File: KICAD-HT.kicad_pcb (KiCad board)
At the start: 2 copper layers, 85 x 70 mm, 124 parts, among them J1 HV80_IN, J2 NAPPE_FILAMENT_HT, Q1 IPD050N10N5, Q2 IPD050N10N5, Q3 BSS127I, Q4 MMBT2222, Q5 BSS127I, T1 MSD1514-103ME, U1 UCC27517, U10 ISO7710, U11 AMC0311R, U12 UCC24612, U13 SN74LVC1G08, U14 TSV791, U15 ATL431, U16 LMV7219, U17 SN74LVC1G132, U18 SN74LVC1G74, U19 ISO7710F, U3 ISO7710, U5 DPC817, U7 AMC0311R, U8 AMC0311R, U9 AMC0302R

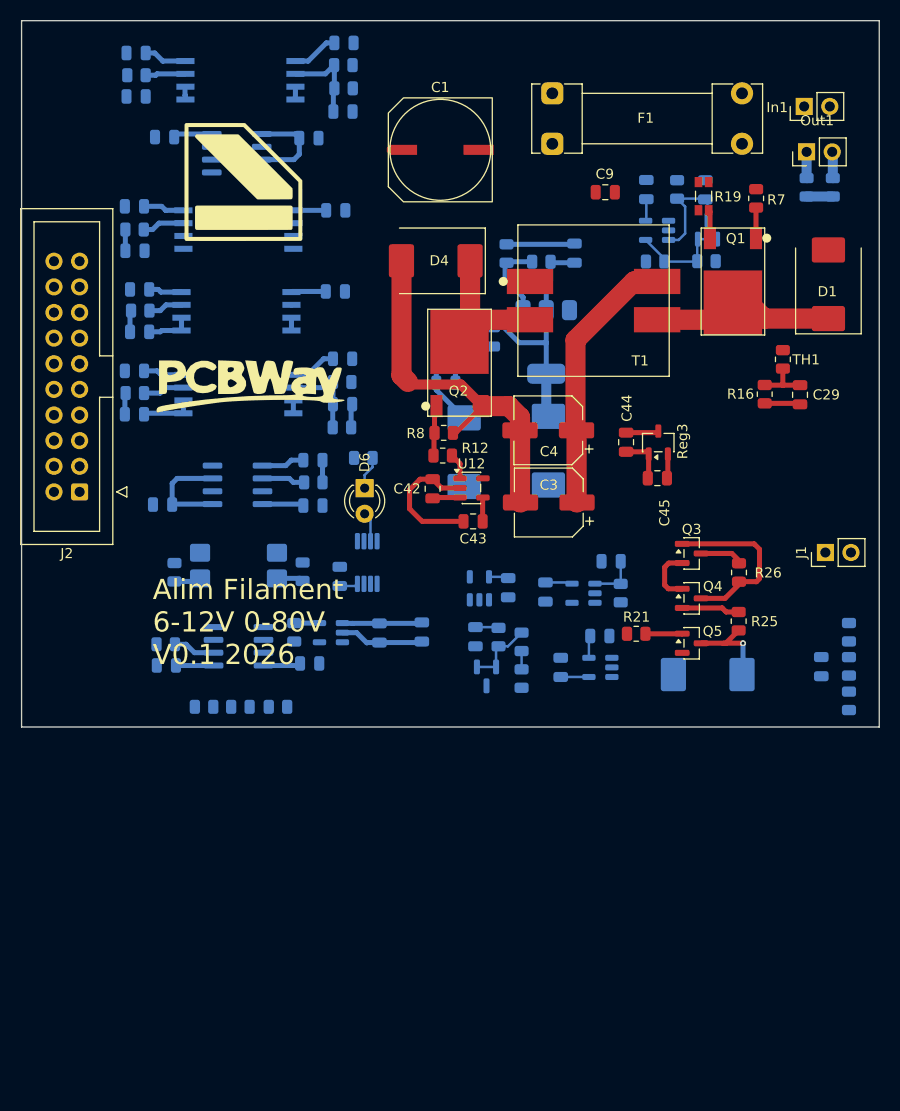
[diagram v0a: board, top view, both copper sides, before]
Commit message: Linearisation HV_BIAS : composants reels en simulation, correctif Rs+Cint
Rejoue la boucle de linearisation (MCP6001 + Q6/Q7) avec des modeles
reels (MMBF170, MCP6001 parametre depuis sa datasheet) plutot que des
modeles ideaux/generiques : revele une oscillation auto-entretenue
invisible sur le schema seul, confirmee independante du proxy MOSFET
et non liee a la bande passante de l'ampli-op (teste avec un TSV791
plus rapide, resultat pire).

Correctif valide en simulation avant report sur le schema : resistance
de degenerescence Rs=330 sur la source de Q6/Q7 (supprime l'oscillation
sans sacrifier l'acces a HV_BIAS=0V) + condensateur de compensation
Cint=1nF autour de l'ampli-op (supprime le depassement en echelon).
Report sur polarisation.kicad_sch et le PCB (R7).

Garde les scripts, modeles et courbes de l'investigation comme
historique de recherche (simulation/*.py, models/, plots/) ; les
sorties volumineuses regenerables (.raw/.csv dans results/) sont
exclues via .gitignore.

Co-Authored-By: Claude Sonnet 5 <noreply@anthropic.com>
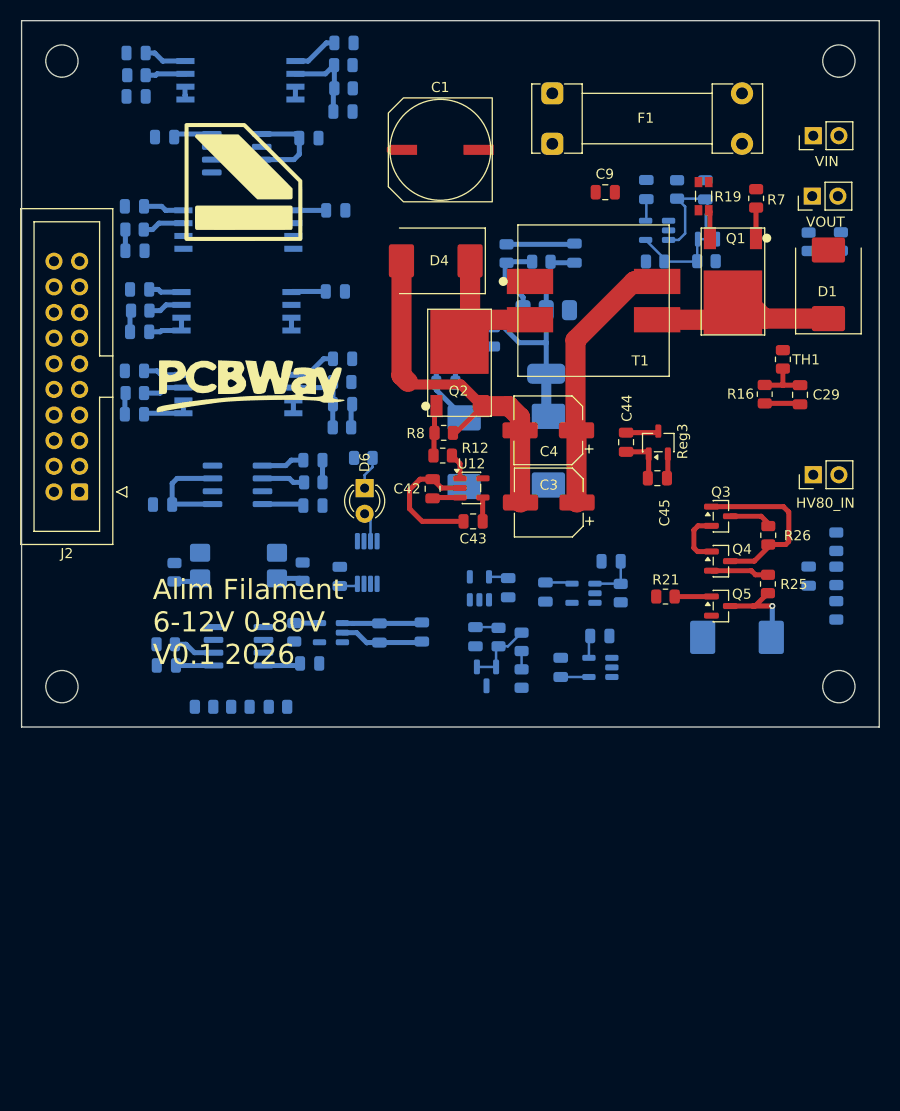
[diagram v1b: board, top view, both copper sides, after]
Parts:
- added ?: , , F.Cu at (176.0, 51.0)
- added ?: , , F.Cu at (176.0, 113.0)
- added REF**: MountingHole_3.2mm_M3, MountingHole:MountingHole_3.2mm_M3, F.Cu at (99.0, 113.0)
- added REF**: MountingHole_3.2mm_M3, MountingHole:MountingHole_3.2mm_M3, F.Cu at (99.0, 51.0)
- moved C27 9.05 mm to (173.0, 102.0)
- moved R40 9.05 mm to (175.7, 98.6)
- moved R41 9.05 mm to (175.7, 102.0)
- moved R42 9.05 mm to (175.7, 105.4)
- moved J1 7.80 mm to (173.5, 92.0)
- moved R10 5.43 mm to (176.2, 68.9)
- moved R9 5.40 mm to (173.0, 68.9)
- moved D3 4.69 mm to (165.9, 108.1)
- moved Q3 4.69 mm to (164.3, 96.1)
- moved Q4 4.69 mm to (164.3, 100.6)
- moved Q5 4.69 mm to (164.3, 105.0)
- moved R26 4.69 mm to (169.0, 98.0)
- moved R21 4.69 mm to (158.8, 104.1)
- moved R25 4.69 mm to (169.0, 102.8)
- moved Out1 4.42 mm to (173.4, 64.4)
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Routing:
- net VOUT_N: track 61.9 -> 59.2 mm
- net VOUT_P: track 34.9 -> 32.3 mm
- net HV_BIAS: track 11.9 -> 9.32 mm

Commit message: Linearisation HV_BIAS : stabilise sous PWM reel (Rs=1k/Cint=100p), placement Q7
Le correctif precedent (Rs=330/Cint=1nF) n'avait ete valide qu'avec un
echelon analogique deja filtre, pas le vrai PWM du C2000. En rejouant la
boucle avec le PWM reel, elargir le filtre d'entree pour ecraser
l'ondulation residuelle (R47/Cin : 1k/1n -> 100k/100n) a reintroduit une
oscillation auto-entretenue differente (~700kHz), confirmee independante
du PWM via un echelon direct isole avant le filtre.

Nouveau correctif, verifie sur le profil complet de commande PWM (3,5s) :
Rs=1k (degenerescence Q6, au lieu de 330) + Cint=100pF (compensation
ampli-op, au lieu de 1nF) -- ondulation residuelle en sortie sous le mV.
Reporte sur polarisation.kicad_sch.

simulation/gen_pwm_breakpoints.py : genere la table PWL explicite
necessaire pour que LTspice resolve correctement les impulsions PWM
etroites -- une expression comportementale IF(TIME...) ne declare aucun
breakpoint, le solveur en sautait ~98% sans elle.

Cote PCB : placement de l'empreinte Q7 (BSS127I, SOT-23) sur la feuille
Polarisation ; isolation.kicad_sch renomme NAPPE_FILAMENT_HT -> DC_HT.

Co-Authored-By: Claude Sonnet 5 <noreply@anthropic.com>
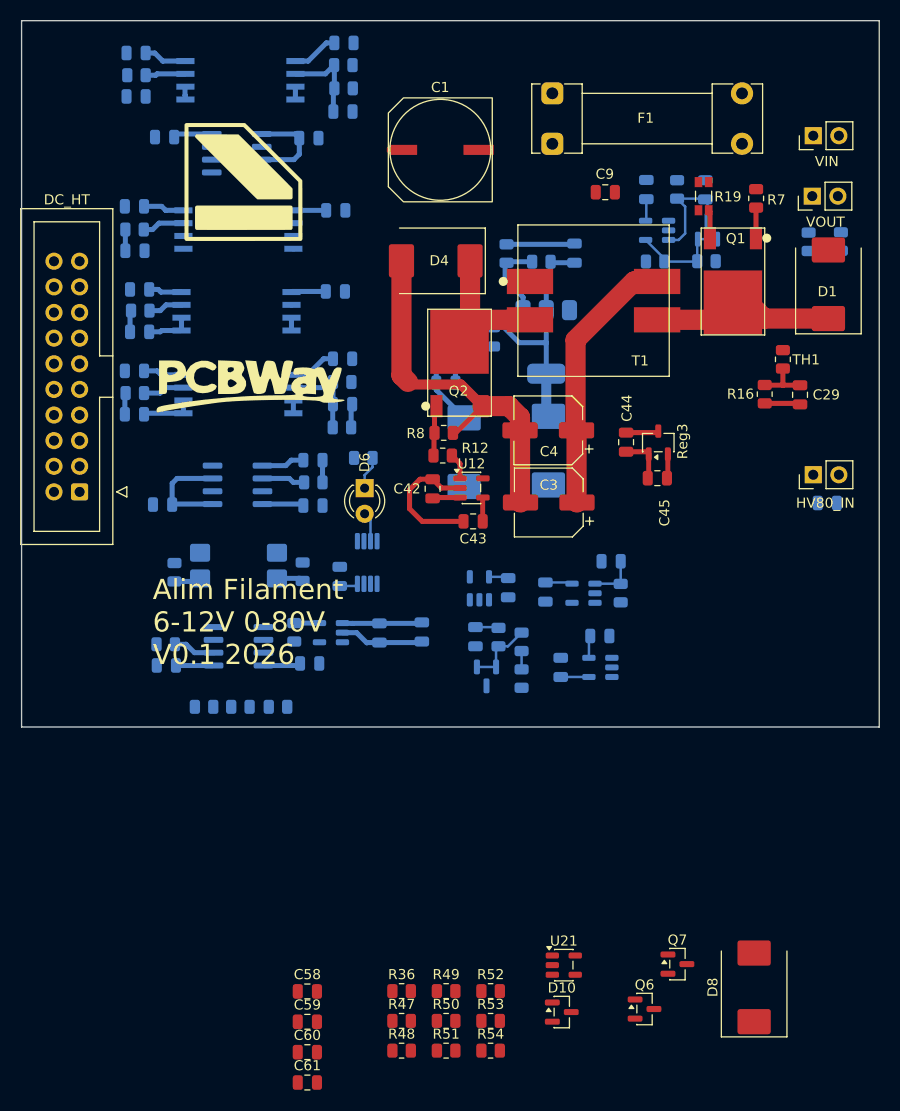
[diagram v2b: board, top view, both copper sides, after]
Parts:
- removed ? (x2): , 
- removed C27: 100n, Capacitor_SMD:C_0805_2012Metric
- removed D3: SMCJ100A, Diode_SMD:D_SMC
- removed Q3, Q5: BSS127I, Package_TO_SOT_SMD:SOT-23
- removed Q4: MMBT2222, Package_TO_SOT_SMD:SOT-23
- removed R21, R40, R41, R42: 1M, Resistor_SMD:R_0805_2012Metric
- removed R25: 2k, Resistor_SMD:R_0805_2012Metric
- removed R26: 75k, Resistor_SMD:R_0805_2012Metric
- removed REF** (x2): MountingHole_3.2mm_M3, MountingHole:MountingHole_3.2mm_M3
- added C58: 100n, Capacitor_SMD:C_0805_2012Metric, F.Cu at (123.3, 143.2)
- added C59: 1u, Capacitor_SMD:C_0805_2012Metric, F.Cu at (123.3, 146.2)
- added C60: 10n, Capacitor_SMD:C_0805_2012Metric, F.Cu at (123.3, 149.2)
- added C61: 1n, Capacitor_SMD:C_0805_2012Metric, F.Cu at (123.3, 152.2)
- added C62: 100n, Capacitor_SMD:C_0805_2012Metric, B.Cu at (174.8, 94.8)
- added D10: BAT54S, Package_TO_SOT_SMD:SOT-23, F.Cu at (148.5, 145.2)
- added D8: SMCJ100A, Diode_SMD:D_SMC, F.Cu at (167.6, 142.8)
- added Q6: BSS127I, Package_TO_SOT_SMD:SOT-23, F.Cu at (156.7, 144.9)
- added Q7: BSS127I, Package_TO_SOT_SMD:SOT-23, F.Cu at (160.0, 140.5)
- added R36: 10k, Resistor_SMD:R_0805_2012Metric, F.Cu at (132.7, 143.2)
- added R47: 1k, Resistor_SMD:R_0805_2012Metric, F.Cu at (132.7, 146.1)
- added R48: 100k, Resistor_SMD:R_0805_2012Metric, F.Cu at (132.7, 149.1)
- added R49: 1k, Resistor_SMD:R_0805_2012Metric, F.Cu at (137.1, 143.2)
- added R50: 100k, Resistor_SMD:R_0805_2012Metric, F.Cu at (137.1, 146.1)
- added R51: 330, Resistor_SMD:R_0805_2012Metric, F.Cu at (137.1, 149.1)
- added R52: 3,9k, Resistor_SMD:R_0805_2012Metric, F.Cu at (141.5, 143.2)
- added R53: 100k, Resistor_SMD:R_0805_2012Metric, F.Cu at (141.5, 146.1)
- added R54: 10k, Resistor_SMD:R_0805_2012Metric, F.Cu at (141.5, 149.1)
- added U21: MCP6001, Package_TO_SOT_SMD:SOT-23-5, F.Cu at (148.7, 140.6)
- J2: value NAPPE_FILAMENT_HT -> DC_HT
- R24: value 100 -> 1k
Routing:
- net CS_GATE: track 17.4 -> 0.00 mm
- net HV_BIAS: track 9.32 -> 0.00 mm, vias 1 -> 0
- net CS_EMIT: track 5.76 -> 0.00 mm
- net CS_TOP: track 5.57 -> 0.00 mm
- net HV80_IN: track 4.43 -> 0.00 mm
- net VAR_GATE: track 5.85 -> 2.20 mm

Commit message: Routage en cours : retouches schema (alim/flyback/isolation/limitation-courant/polarisation), doc renommage Temp_ht->I_Out_ht et NAPPE_FILAMENT_HT->DC_HT, fix .kicad_dru (commentaires #), nettoyage simulation/results
Co-Authored-By: Claude Sonnet 5 <noreply@anthropic.com>
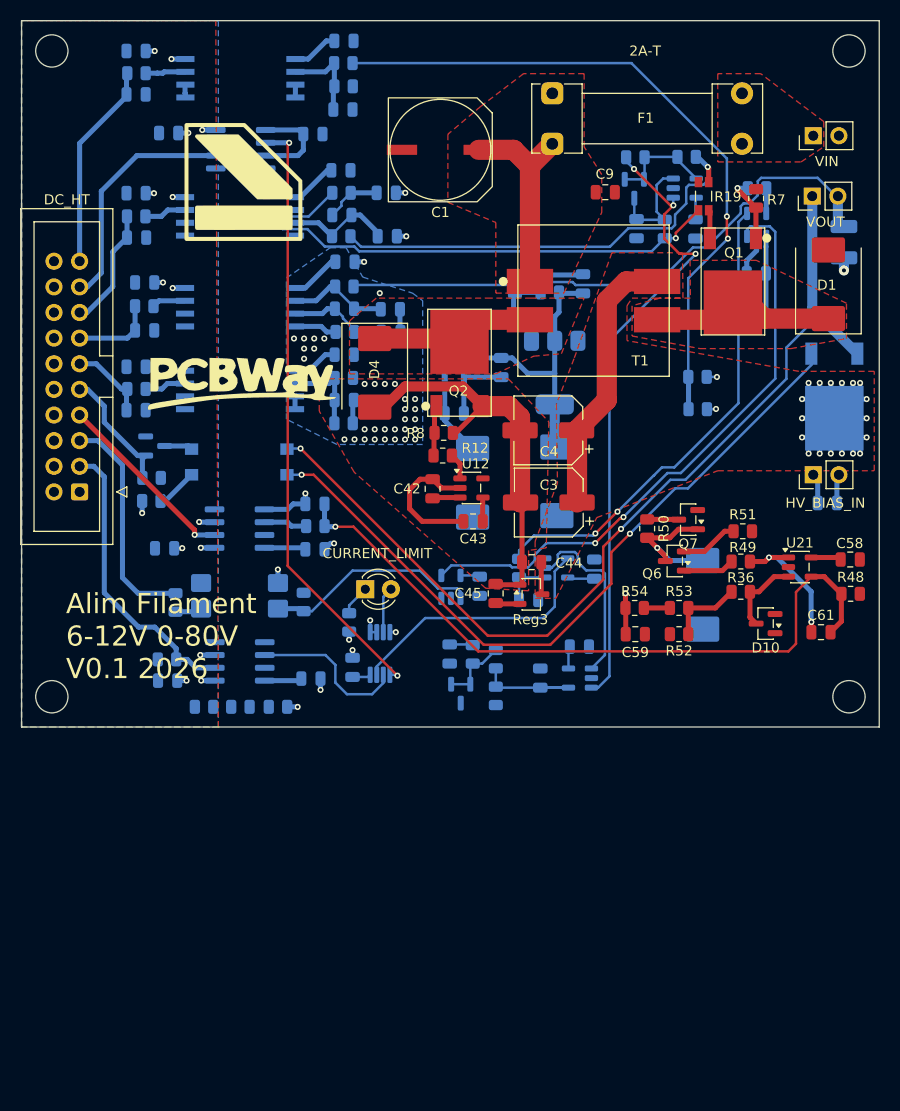
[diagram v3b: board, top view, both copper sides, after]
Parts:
- removed C25, C26: 100n, Capacitor_SMD:C_0805_2012Metric
- removed C29: 100p, Capacitor_SMD:C_0805_2012Metric
- removed C30: 1n, Capacitor_SMD:C_0805_2012Metric
- removed R16: 10k, Resistor_SMD:R_0805_2012Metric
- removed R17: 100, Resistor_SMD:R_0805_2012Metric
- removed R47: 1k, Resistor_SMD:R_0805_2012Metric
- removed TH1: 10k_B4000, Resistor_SMD:R_0805_2012Metric
- removed U8: AMC0311R, SOIC_DWV:SOIC-8_DWV_5.85x11.5mm_P1.27mm
- added C37: 100n, Capacitor_SMD:C_0805_2012Metric, B.Cu at (127.0, 70.9)
- added C49: 100n, Capacitor_SMD:C_0805_2012Metric, B.Cu at (107.2, 72.9)
- added C63: 10n, Capacitor_SMD:C_0805_2012Metric, B.Cu at (127.0, 75.5)
- added C64: 1n, Capacitor_SMD:C_0805_2012Metric, B.Cu at (131.6, 75.6)
- added C65: 1n, Capacitor_SMD:C_0805_2012Metric, B.Cu at (131.6, 77.8)
- added C66: 1n, Capacitor_SMD:C_0805_2012Metric, B.Cu at (131.2, 68.4)
- added C67: 10n, Capacitor_SMD:C_0805_2012Metric, B.Cu at (126.7, 66.3)
- added C68: 1n, Capacitor_SMD:C_0805_2012Metric, B.Cu at (131.1, 64.1)
- added Q4: MMBF170, Package_TO_SOT_SMD:SOT-23, B.Cu at (108.2, 89.2)
- added Q5: IPD60R360P7, TO252:TO252-3_TabPin2, B.Cu at (175.6, 84.3)
- added R21: 100k, Resistor_SMD:R_0805_2012Metric, B.Cu at (107.9, 92.3)
- added R25: 10m, Resistor_SMD:R_1210_3225Metric_Pad1.30x2.65mm_HandSolder, B.Cu at (176.5, 69.0)
- added R26: 1k, Resistor_SMD:R_0805_2012Metric, B.Cu at (107.2, 75.3)
- added R35: 150, Resistor_SMD:R_0805_2012Metric, B.Cu at (107.9, 94.6)
- added R40: 10, Resistor_SMD:R_0805_2012Metric, B.Cu at (127.0, 73.3)
- added R41: 10, Resistor_SMD:R_0805_2012Metric, B.Cu at (127.0, 77.8)
- added R42: 10, Resistor_SMD:R_0805_2012Metric, B.Cu at (126.7, 64.1)
- added R43: 10, Resistor_SMD:R_0805_2012Metric, B.Cu at (126.7, 68.4)
- added REF**: MountingHole_3.2mm_M3, MountingHole:MountingHole_3.2mm_M3, F.Cu at (177.0, 114.0)
- added REF**: MountingHole_3.2mm_M3, MountingHole:MountingHole_3.2mm_M3, F.Cu at (177.0, 50.0)
- added REF**: MountingHole_3.2mm_M3, MountingHole:MountingHole_3.2mm_M3, F.Cu at (98.0, 114.0)
- added REF**: MountingHole_3.2mm_M3, MountingHole:MountingHole_3.2mm_M3, F.Cu at (98.0, 50.0)
- added U20: VODA1275, VODA1275:SMD-4_VODA1275_VIS, B.Cu at (116.6, 90.7)
- added U22: AMC0302R, SOIC_DWV:SOIC-8_DWV_5.85x11.5mm_P1.27mm, B.Cu at (116.7, 75.4)
- C41: value 1n -> 100n
- C60: value 10n -> 47n; moved to B.Cu
- C61: value 1n -> 100p
- D6: value LED -> CURRENT_LIMIT
- D8: moved to B.Cu
- F1: value 3A -> 2A-T
- J1: value HV80_IN -> HV_BIAS_IN
- R24: value 1k -> 100k
- R51: value 330 -> 1k
- moved C60 73.3 mm to (107.2, 77.7)
- moved C58 68.8 mm to (177.1, 100.4)
- moved C61 67.7 mm to (174.2, 107.6)
- moved R11 63.6 mm to (167.9, 63.6), turned to 180 degrees
- moved R48 63.5 mm to (177.2, 103.8)
- moved R51 59.3 mm to (166.5, 97.6)
- moved U1 58.4 mm to (167.8, 67.2), turned to 90 degrees
- moved R50 52.7 mm to (157.0, 97.3), turned to -90 degrees
- moved R36 51.9 mm to (166.3, 103.6)
- moved R49 51.6 mm to (166.3, 100.6)
- moved C19 51.6 mm to (167.8, 72.0), turned to 180 degrees
- moved C59 50.3 mm to (155.8, 107.8)
- moved R54 46.1 mm to (155.8, 105.2)
- moved U21 45.9 mm to (172.1, 101.2)
- moved C21 45.7 mm to (167.9, 76.2), turned to 180 degrees
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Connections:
- net HV80_IN renamed HV_BIAS_IN
- net HV_BIAS renamed HV_BIAS_OUT
- C60 pad 1: Net-(D8-A2) -> I_Out_ht
- C60 pad 2: GND -> GND_CTRL
- C61 pad 2: Net-(U21-IN-) -> VAR_GATE
- J2 pad 13: Temp_ht -> I_Out_ht
- Out1 pad 1: VOUT_P -> V_HT_OUT
- Out1 pad 2: VOUT_N -> ISNS_P
- R48 pad 1: Net-(U21-IN-) -> VAR_GATE
- U21 pad 4: Net-(U21-IN-) -> VAR_GATE
- U9 pad 2: ISNS_KP -> Net-(U9-INP)
- U9 pad 3: ISNS_KN -> Net-(U9-INN)
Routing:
- net V_HT_OUT: track 0.00 -> 95.2 mm, vias 0 -> 2
- net U15_OUTP: track 0.00 -> 73.4 mm, vias 0 -> 2
- net HV_BIAS_OUT: track 0.00 -> 71.6 mm, vias 0 -> 3
- net VAR_GATE: track 2.20 -> 69.6 mm, vias 0 -> 1
- net PWM_PRI_OUT: track 0.00 -> 63.4 mm, vias 0 -> 2
- net ISNS_AMP: track 0.00 -> 62.7 mm, vias 0 -> 3
- net ~{Q_TRIP}: track 0.00 -> 60.5 mm, vias 0 -> 2
- net ISNS_P: track 0.00 -> 60.4 mm
- net EN_PRI_GATED: track 0.00 -> 60.0 mm, vias 0 -> 2
- net ISNS_KP: track 0.00 -> 51.3 mm, vias 0 -> 1
- net ISNS_KN: track 0.00 -> 44.6 mm, vias 0 -> 1
- net ~{PRE}: track 0.00 -> 26.2 mm
- net PWM_ht: track 4.17 -> 29.0 mm
- net I_Shunt_ht_comp: track 0.00 -> 23.4 mm
- net PWM_EN: track 0.00 -> 22.3 mm
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- added copper zone on In2.Cu, net 3V3_ISO
- added copper zone on In1.Cu, net GND
- added copper zone on B.Cu, net GND_CTRL
- added copper zone on F.Cu, net GND_CTRL
- added copper zone on In1.Cu, net GND_CTRL
- added copper zone on F.Cu, net Net-(In1-Pin_1)
- added copper zone on F.Cu, net SW_PRI
- added copper zone on F.Cu, net SW_SEC
- added copper zone on F.Cu, net VIN
- added copper zone on B.Cu, net VOUT_N
- added copper zone on F.Cu, net VOUT_N
- added copper zone on In1.Cu, net VOUT_N
- added copper zone on F.Cu, net VOUT_P
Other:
- copper layers 2 -> 4
